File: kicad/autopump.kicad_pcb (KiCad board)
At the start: 2 copper layers, 62.2 x 66 mm, 12 parts, among them P1 HE10-16, P2 CONN_01X03, P3 CONN_01X06, P4 CONN_01X16, SW1 SW_PUSH, SW2 SW_PUSH

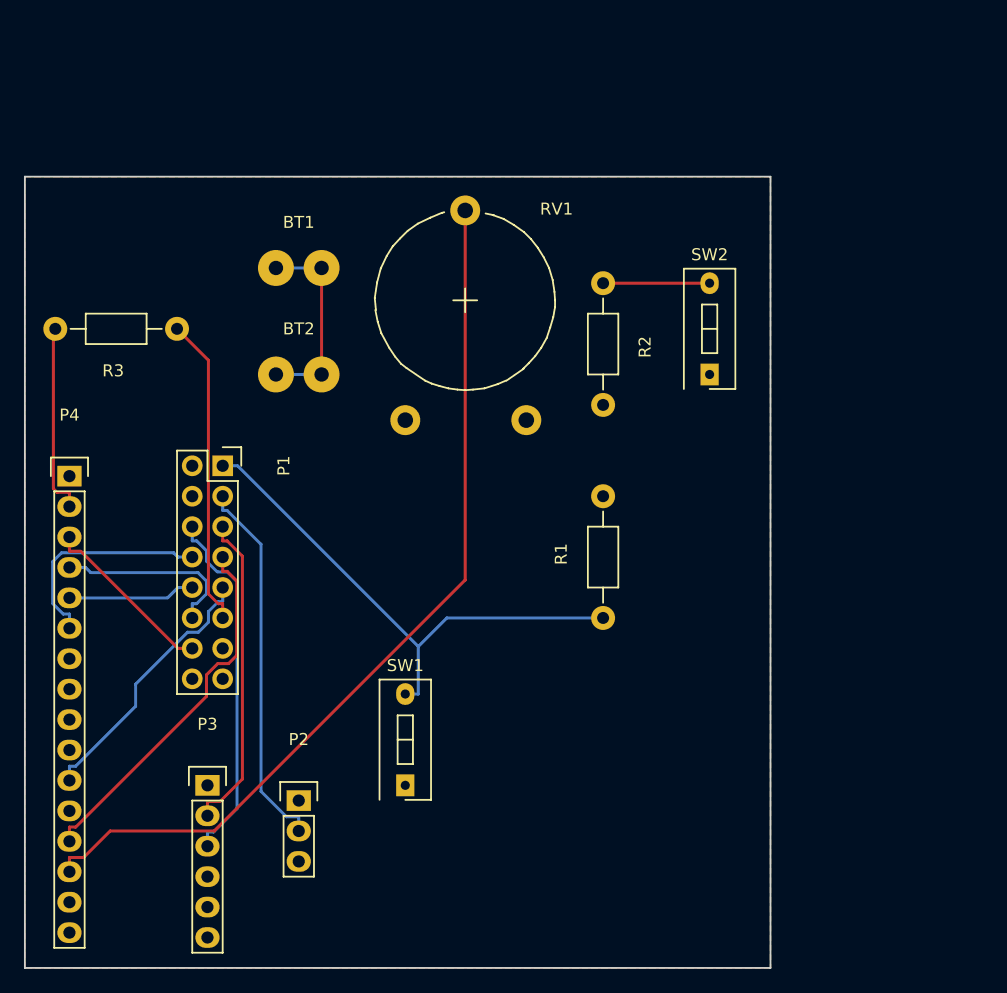
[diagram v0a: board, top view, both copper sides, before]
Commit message: More work on the PCB. - make use of the and Arduino shield (http://www.thingiverse.com/thing:9630) library. - reorganize layouts of components - changed the track width and clearances a bit wider - added my name, URL and OSHW logo to PCB
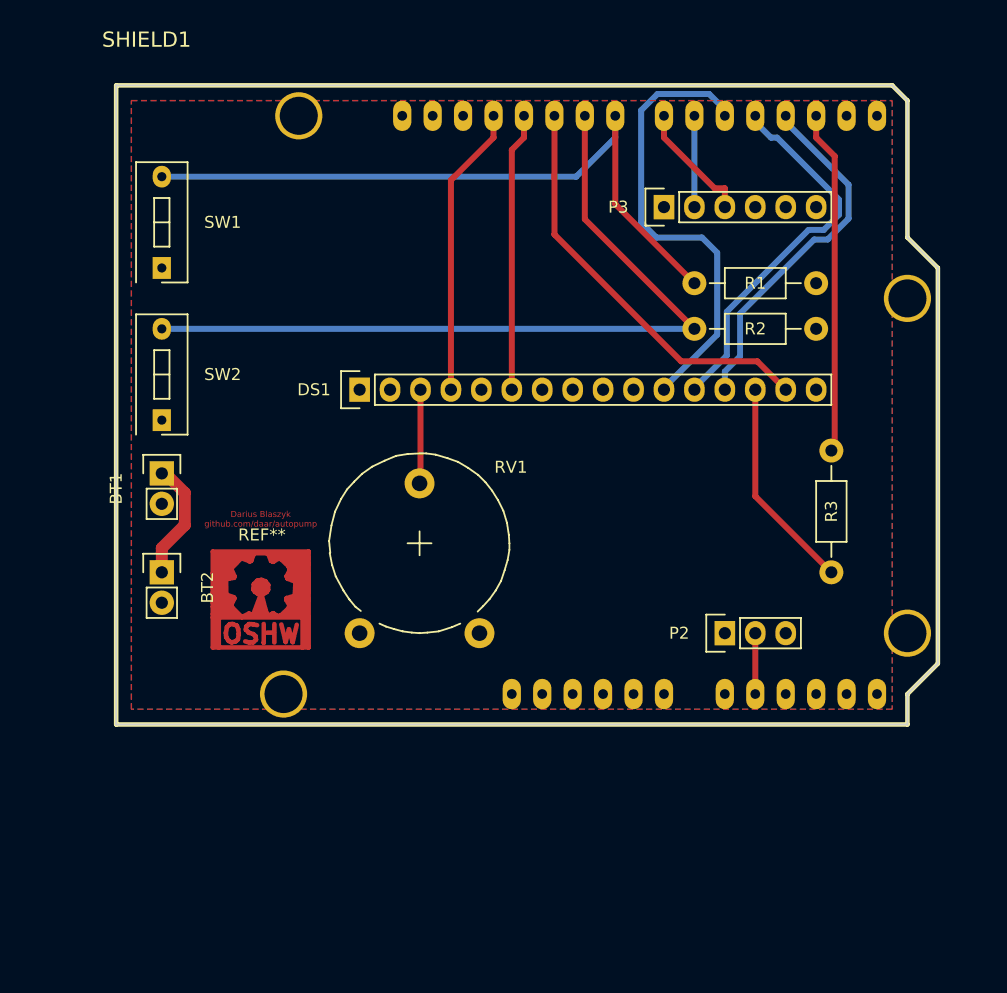
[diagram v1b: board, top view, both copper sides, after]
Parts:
- removed P1: HE10-16, Socket_Strips:Socket_Strip_Straight_2x08
- removed P4: CONN_01X16, Pin_Headers:Pin_Header_Straight_1x16
- added DS1: LCD16X2, Socket_Strips:Socket_Strip_Straight_1x16, F.Cu at (133.3, 102.9)
- added REF**: Symbol_OSHW-Logo_CopperTop_Negative, Symbols:Symbol_OSHW-Logo_CopperTop_Negative, F.Cu at (125.1, 119.4)
- added SHIELD1: ARDUINO_SHIELD, arduino_shields:ARDUINO SHIELD, F.Cu at (113.0, 130.8)
- BT1, BT2: footprint Wire_Pads:SolderWirePad_2x_1-2mmDrill -> Socket_Strips:Socket_Strip_Straight_1x02
- P2: footprint Pin_Headers:Pin_Header_Straight_1x03 -> Socket_Strips:Socket_Strip_Straight_1x03
- P3: footprint Pin_Headers:Pin_Header_Straight_1x06 -> Socket_Strips:Socket_Strip_Straight_1x06
- RV1: footprint Potentiometers:Potentiometer_Trimmer-Piher_PT15-V17-5_horizontal -> Potentiometers:Potentiometer_Trimmer-Piher_PT15-V12-5_horizontal
- moved P3 61.5 mm to (158.8, 87.6)
- moved R3 55.5 mm to (172.7, 108.0), turned to 270 degrees
- moved SW1 47.7 mm to (116.8, 92.7)
- moved SW2 45.9 mm to (116.8, 105.4)
- moved P2 38.2 mm to (163.8, 123.2)
- moved R1 29.0 mm to (161.3, 94.0), turned to 0 degrees
- moved BT1 20.6 mm to (116.8, 109.9), turned to 270 degrees
- moved BT2 20.1 mm to (116.8, 118.1), turned to 270 degrees
- moved RV1 18.2 mm to (133.3, 123.2)
- moved R2 8.52 mm to (161.3, 97.8), turned to 0 degrees
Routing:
- net Net-(DS1-Pad3): track 74.7 -> 7.85 mm
- net Net-(R2-Pad1): track 8.89 -> 66.0 mm
- net Net-(DS1-Pad11): track 0.00 -> 38.6 mm
- net Net-(DS1-Pad15): track 0.00 -> 34.6 mm
- net Net-(DS1-Pad12): track 0.00 -> 31.8 mm
- net Net-(P1-Pad7): track 31.1 -> 0.00 mm
- net Net-(DS1-Pad13): track 0.00 -> 30.0 mm
- net Net-(P2-Pad2): track 31.4 -> 5.08 mm
- net Net-(DS1-Pad4): track 0.00 -> 24.3 mm
- net Net-(DS1-Pad6): track 0.00 -> 23.3 mm
- net Net-(P1-Pad9): track 22.5 -> 0.00 mm
- net Net-(P3-Pad3): track 30.3 -> 10.2 mm
- net Net-(P3-Pad2): track 26.8 -> 7.62 mm
- net Net-(P1-Pad8): track 18.5 -> 0.00 mm
- net Net-(P1-Pad12): track 15.7 -> 0.00 mm
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- added copper zone on F.Cu, net +5V
- added copper zone on B.Cu, net GND
- removed copper zone on B.Cu, net +5V
- removed copper zone on F.Cu, net GND
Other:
- board size 62.2 x 66 mm -> 68.6 x 53.3 mm
- net class Default: clearance 0.2 -> 0.3; trace_width 0.25 -> 0.5
- net class Power 12V added: clearance 0.4, trace_width 1, via_dia 1, via_drill 0.4
- rule trace_clearance: 0.2 -> 0.3
- board text added: "Darius Blaszyk github.com/daar/autopump"

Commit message: More work on the schema and PCB   - fixed and reorganized the power supply in the schema   - changed the footprints to be more suitable   - reorgnized the footprints slightly on the PCB for better layout and connectivity
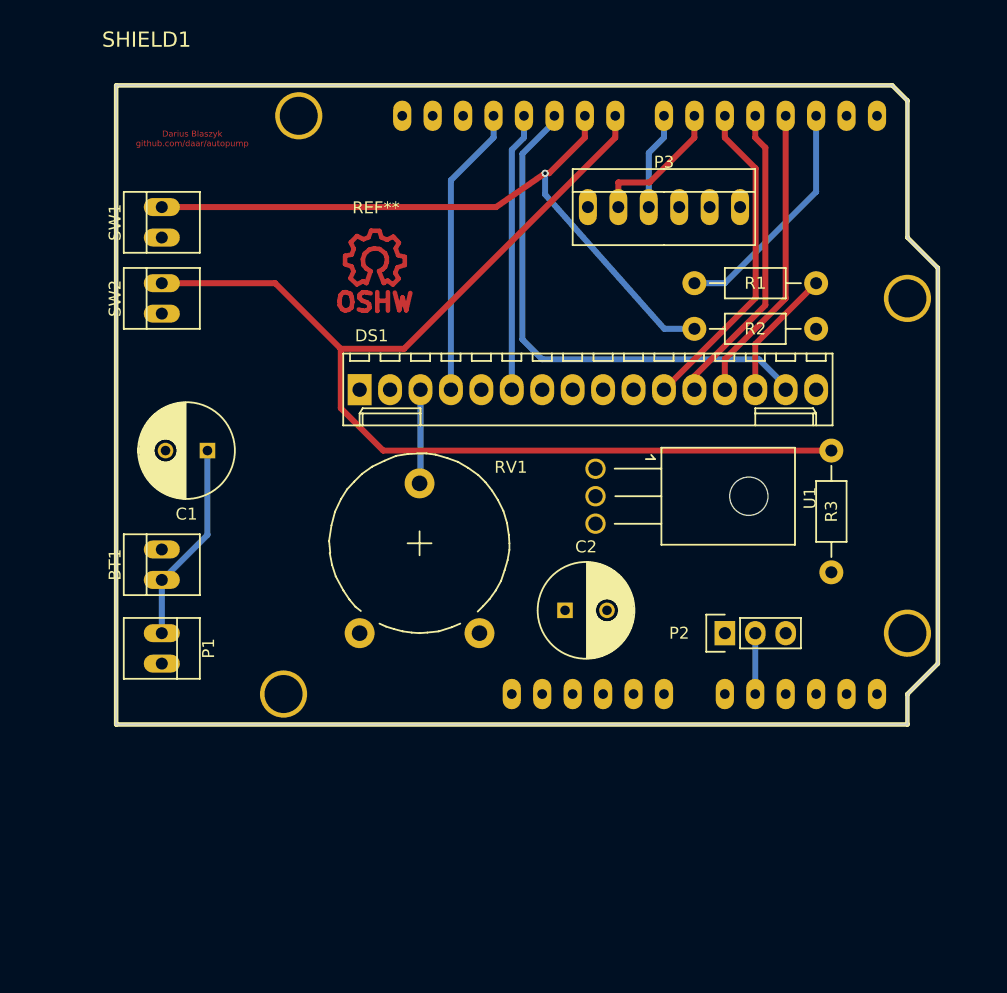
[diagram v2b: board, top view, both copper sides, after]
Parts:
- removed BT2: Battery, Socket_Strips:Socket_Strip_Straight_1x02
- removed the REF** at (125.1, 119.4)
- added C1: 0.33uF, Capacitors_ThroughHole:C_Radial_D8_L11.5_P3.5, F.Cu at (120.7, 108.0)
- added C2: 0.1uF, Capacitors_ThroughHole:C_Radial_D8_L11.5_P3.5, F.Cu at (150.5, 121.3)
- added P1: Relay power, Connect:PINHEAD1-2, F.Cu at (116.8, 124.5)
- added REF**: Symbol_OSHW-Logo_CopperTop, Symbols:Symbol_OSHW-Logo_CopperTop, F.Cu at (134.6, 92.1)
- added U1: LM7805, TO_SOT_Packages_THT:SOT126_SOT32_Housing_Horizontal, F.Cu at (153.0, 111.8)
- BT1: footprint Socket_Strips:Socket_Strip_Straight_1x02 -> Connect:PINHEAD1-2
- DS1: footprint Socket_Strips:Socket_Strip_Straight_1x16 -> Connectors_Molex:Molex_KK-6410-16_16x2.54mm_Straight
- P2: value CONN_01X03 -> Pressure transducer
- P3: value CONN_01X06 -> Relay control; footprint Socket_Strips:Socket_Strip_Straight_1x06 -> Connect:PINHEAD1-6
- R1: value 10k -> 33k
- R3: value 33k -> 10k
- SW1: value SW_PUSH -> Button 1; footprint Buttons_Switches_ThroughHole:SW_DIP_x1_Slide -> Connect:PINHEAD1-2
- SW2: value SW_PUSH -> Button 2; footprint Buttons_Switches_ThroughHole:SW_DIP_x1_Slide -> Connect:PINHEAD1-2
- moved SW2 10.2 mm to (116.8, 95.2), turned to 90 degrees
- moved BT1 7.62 mm to (116.8, 117.5), turned to 90 degrees
- moved SW1 3.81 mm to (116.8, 88.9), turned to 90 degrees
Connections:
- BT1 pad 1: +12V -> Net-(BT1-Pad1)
- DS1 pad 10: Net-(DS1-Pad10) -> (no net)
- DS1 pad 2: +5V -> 5V
- DS1 pad 7: Net-(DS1-Pad7) -> (no net)
- DS1 pad 8: Net-(DS1-Pad8) -> (no net)
- DS1 pad 9: Net-(DS1-Pad9) -> (no net)
- P2 pad 1: +5V -> 5V
- P3 pad 1: +5V -> 5V
- P3 pad 4: Net-(P3-Pad4) -> (no net)
- P3 pad 5: Net-(P3-Pad5) -> (no net)
- R1 pad 2: GND -> Net-(DS1-Pad14)
- R3 pad 2: Net-(DS1-Pad14) -> GND
- RV1 pad 1: +5V -> 5V
- SHIELD1 pad 0: Net-(SHIELD1-Pad0) -> (no net)
- SHIELD1 pad 1: Net-(SHIELD1-Pad1) -> (no net)
- SHIELD1 pad 13: Net-(SHIELD1-Pad13) -> (no net)
- SHIELD1 pad 2: Net-(R3-Pad1) -> Net-(R1-Pad1)
- SHIELD1 pad 3V3: Net-(SHIELD1-Pad3V3) -> (no net)
- SHIELD1 pad 5V: Net-(SHIELD1-Pad5V) -> 5V
- SHIELD1 pad 8: Net-(R1-Pad1) -> Net-(R3-Pad1)
- SHIELD1 pad AD0: Net-(SHIELD1-PadAD0) -> (no net)
- SHIELD1 pad AD2: Net-(SHIELD1-PadAD2) -> (no net)
- SHIELD1 pad AD3: Net-(SHIELD1-PadAD3) -> (no net)
- SHIELD1 pad AD4: Net-(SHIELD1-PadAD4) -> (no net)
- SHIELD1 pad AD5: Net-(SHIELD1-PadAD5) -> (no net)
- SHIELD1 pad AREF: Net-(SHIELD1-PadAREF) -> (no net)
- SHIELD1 pad GND1: Net-(SHIELD1-PadGND1) -> GND
- SHIELD1 pad GND2: Net-(SHIELD1-PadGND2) -> (no net)
- SHIELD1 pad GND3: Net-(SHIELD1-PadGND3) -> (no net)
- SHIELD1 pad RST: Net-(SHIELD1-PadRST) -> (no net)
- SHIELD1 pad V_IN: Net-(SHIELD1-PadV_IN) -> (no net)
- SW1 pad 1: +5V -> 5V
- SW1 pad 2: Net-(R1-Pad1) -> Net-(R2-Pad1)
- SW2 pad 1: +5V -> 5V
- SW2 pad 2: Net-(R2-Pad1) -> Net-(R3-Pad1)
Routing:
- net Net-(R3-Pad1): track 28.7 -> 96.6 mm
- net Net-(R1-Pad1): track 57.7 -> 19.7 mm
- net Net-(BT1-Pad1): track 0.00 -> 16.9 mm
- net Net-(DS1-Pad11): track 38.6 -> 27.1 mm
- net +12V: track 10.0 -> 0.00 mm
- net Net-(DS1-Pad15): track 34.6 -> 43.7 mm
- net Net-(R2-Pad1): track 66.0 -> 58.5 mm, vias 0 -> 1
- net Net-(DS1-Pad14): track 17.9 -> 11.0 mm
- net Net-(DS1-Pad12): track 31.8 -> 25.7 mm
- net Net-(DS1-Pad13): track 30.0 -> 25.0 mm
- net Net-(P3-Pad2): track 7.62 -> 11.8 mm
- net Net-(P3-Pad3): track 10.2 -> 8.15 mm
- added copper zone on F.Cu, net 5V
- removed copper zone on F.Cu, net +5V

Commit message: Removed some unneeded kicad files from github Replaced LM7805 component by the LM7805CT component Added +12V symbol to schema so the PCB design rules work again. Issue #4 Reorganized the board a bit to get a better layout. No vias needed and all power traces on the front Relocated the OSHW logo and text box to a more suitable location Resolved issue #5: connections to the side and using a Phoenix terminal block for the pressure transducer Added a printout of the PCB rendering to github Renamed autopump.pdf to autopump_pcb.pdf
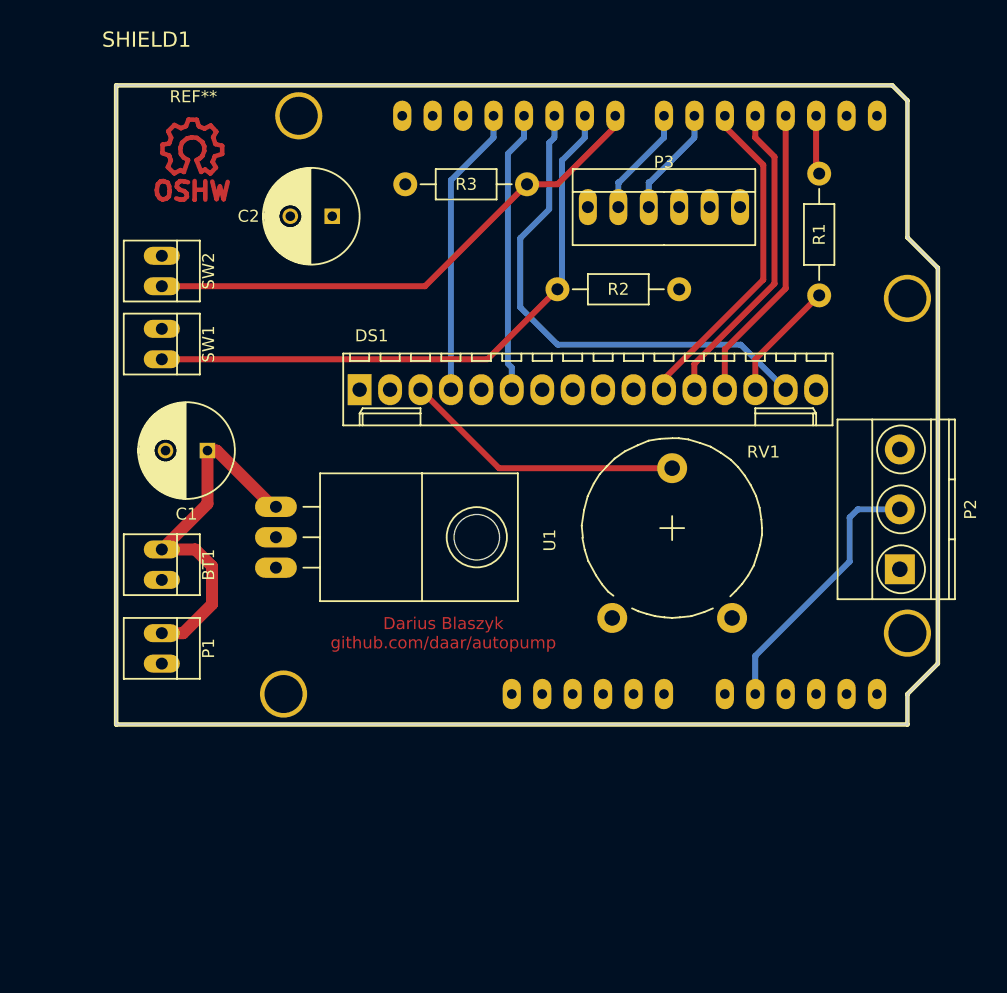
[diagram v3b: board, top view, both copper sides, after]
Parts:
- P2: footprint Socket_Strips:Socket_Strip_Straight_1x03 -> Terminal_Blocks:TerminalBlock_Pheonix_MKDS1.5-3pol
- U1: value LM7805 -> LM7805CT; footprint TO_SOT_Packages_THT:SOT126_SOT32_Housing_Horizontal -> TO_SOT_Packages_THT:TO-220_Neutral123_Horizontal_LargePads
- moved C2 38.2 mm to (131.1, 88.4), turned to 180 degrees
- moved R3 33.8 mm to (147.3, 85.7), turned to 180 degrees
- moved U1 26.9 mm to (126.4, 115.2)
- moved RV1 21.1 mm to (154.4, 121.9)
- moved REF** 17.8 mm to (119.4, 82.8)
- moved P2 15.5 mm to (178.4, 117.9), turned to 90 degrees
- moved R1 13.9 mm to (171.7, 84.8), turned to 270 degrees
- moved R2 11.9 mm to (149.9, 94.5)
- moved SW1 10.2 mm to (116.8, 99.1), turned to 270 degrees
- moved SW2 2.29 mm to (116.8, 93.0), turned to 270 degrees
- turned BT1 to 270 degrees
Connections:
- BT1 pad 1: Net-(BT1-Pad1) -> +12V
- C1 pad 1: Net-(BT1-Pad1) -> +12V
- P1 pad 1: Net-(BT1-Pad1) -> +12V
- SHIELD1 pad 6: Net-(P3-Pad2) -> Net-(P3-Pad3)
- SHIELD1 pad 7: Net-(P3-Pad3) -> Net-(P3-Pad2)
- U1 pad 1: (no net) -> +12V
- U1 pad 2: (no net) -> GND
- U1 pad 3: (no net) -> 5V
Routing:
- net Net-(R3-Pad1): track 96.6 -> 44.3 mm
- net +12V: track 0.00 -> 30.7 mm
- net Net-(P2-Pad2): track 5.08 -> 22.5 mm
- net Net-(BT1-Pad1): track 16.9 -> 0.00 mm
- net Net-(DS1-Pad3): track 7.85 -> 23.7 mm
- net Net-(R1-Pad1): track 19.7 -> 5.29 mm
- net Net-(R2-Pad1): track 58.5 -> 51.0 mm, vias 1 -> 0
- net Net-(P3-Pad2): track 11.8 -> 9.24 mm
- net Net-(DS1-Pad15): track 43.7 -> 42.2 mm
- net Net-(P3-Pad3): track 8.15 -> 9.24 mm
- net Net-(DS1-Pad14): track 11.0 -> 10.1 mm
- net Net-(DS1-Pad12): track 25.7 -> 26.3 mm
- net Net-(DS1-Pad11): track 27.1 -> 27.6 mm
